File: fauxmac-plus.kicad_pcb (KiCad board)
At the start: 2 copper layers, 86.5 x 89 mm, 45 parts, among them J1 oled, K1 KEYSW, K10 KEYSW, K11 KEYSW, K12 KEYSW, K2 KEYSW, K3 KEYSW, K4 KEYSW, K5 KEYSW, K6 KEYSW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

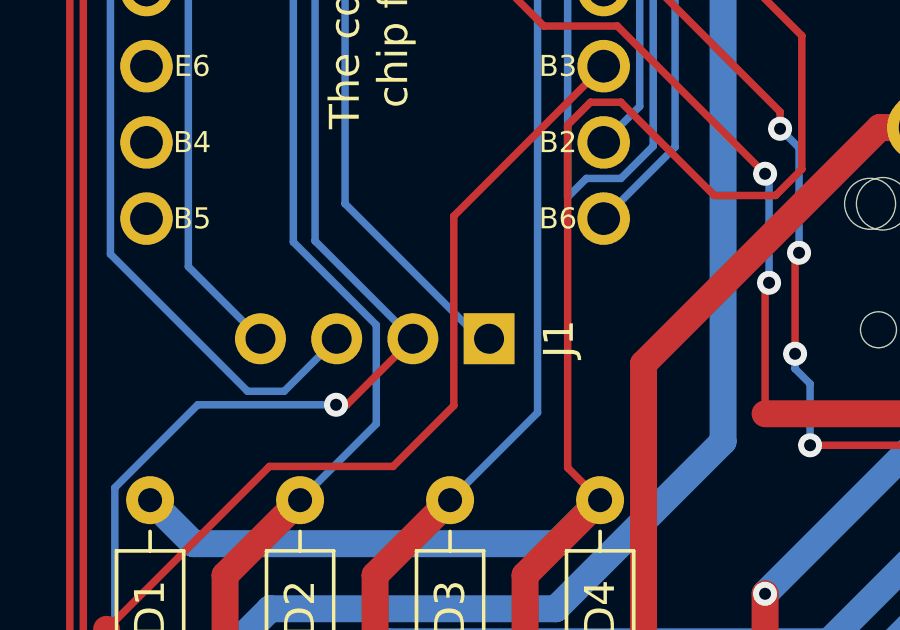
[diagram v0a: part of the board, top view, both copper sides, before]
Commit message: amend oled labelling, regen gerbers
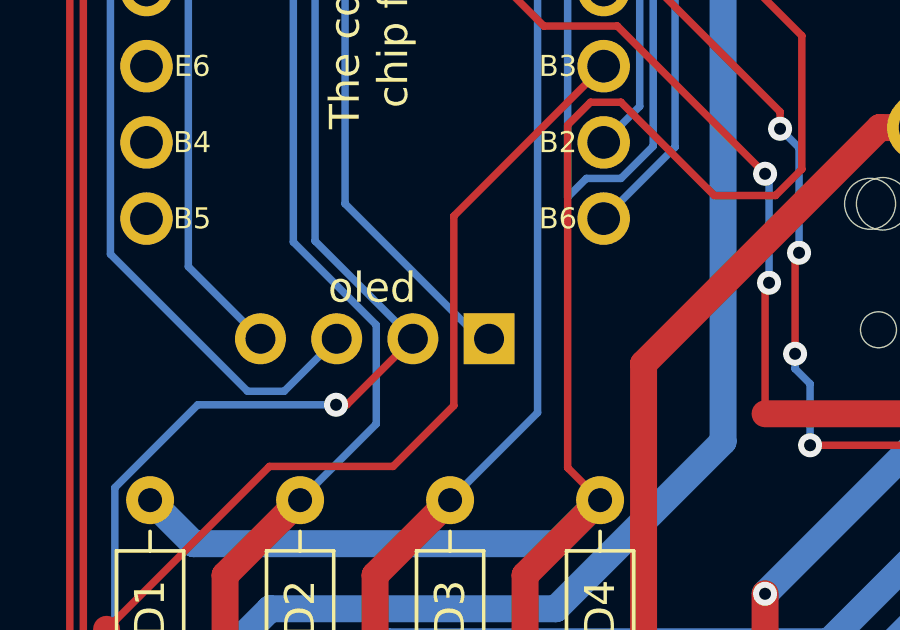
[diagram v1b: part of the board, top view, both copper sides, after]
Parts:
- renumbered J1 to oled
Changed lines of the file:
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@@
       (sketchpadsonfab false)
       (subtractmaskfromsilk false)
-      (outputformat 3)
+      (outputformat 1)
       (mirror false)
       (drillshape 0)
@@
     (property "Sheetname" "")
     (attr through_hole)
-    (fp_text reference "J1" (at 0 -2.33 90) (layer "F.SilkS")
-      (effects (font (size 1 1) (thickness 0.15)))
-    )
+    (fp_text reference "oled" (at -1.7 3.9 180) (layer "F.SilkS")
+      (effects (font (size 1 1) (thickness 0.15)))
+    )
